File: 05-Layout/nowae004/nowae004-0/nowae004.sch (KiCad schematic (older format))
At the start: 14 parts

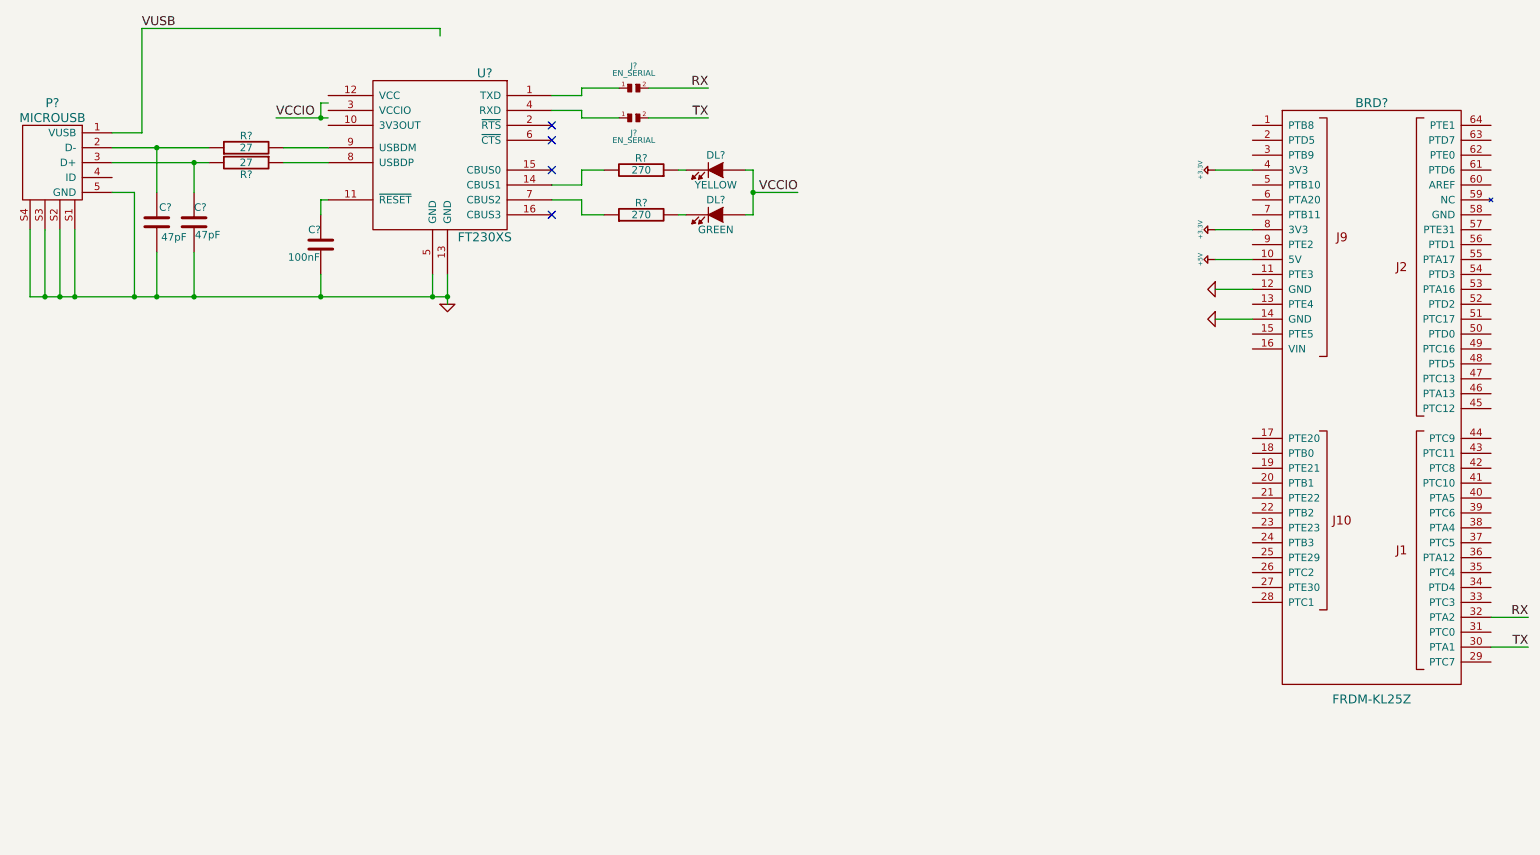
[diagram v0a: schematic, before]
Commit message: Added spare LEDs, protection for power supply and some component informations
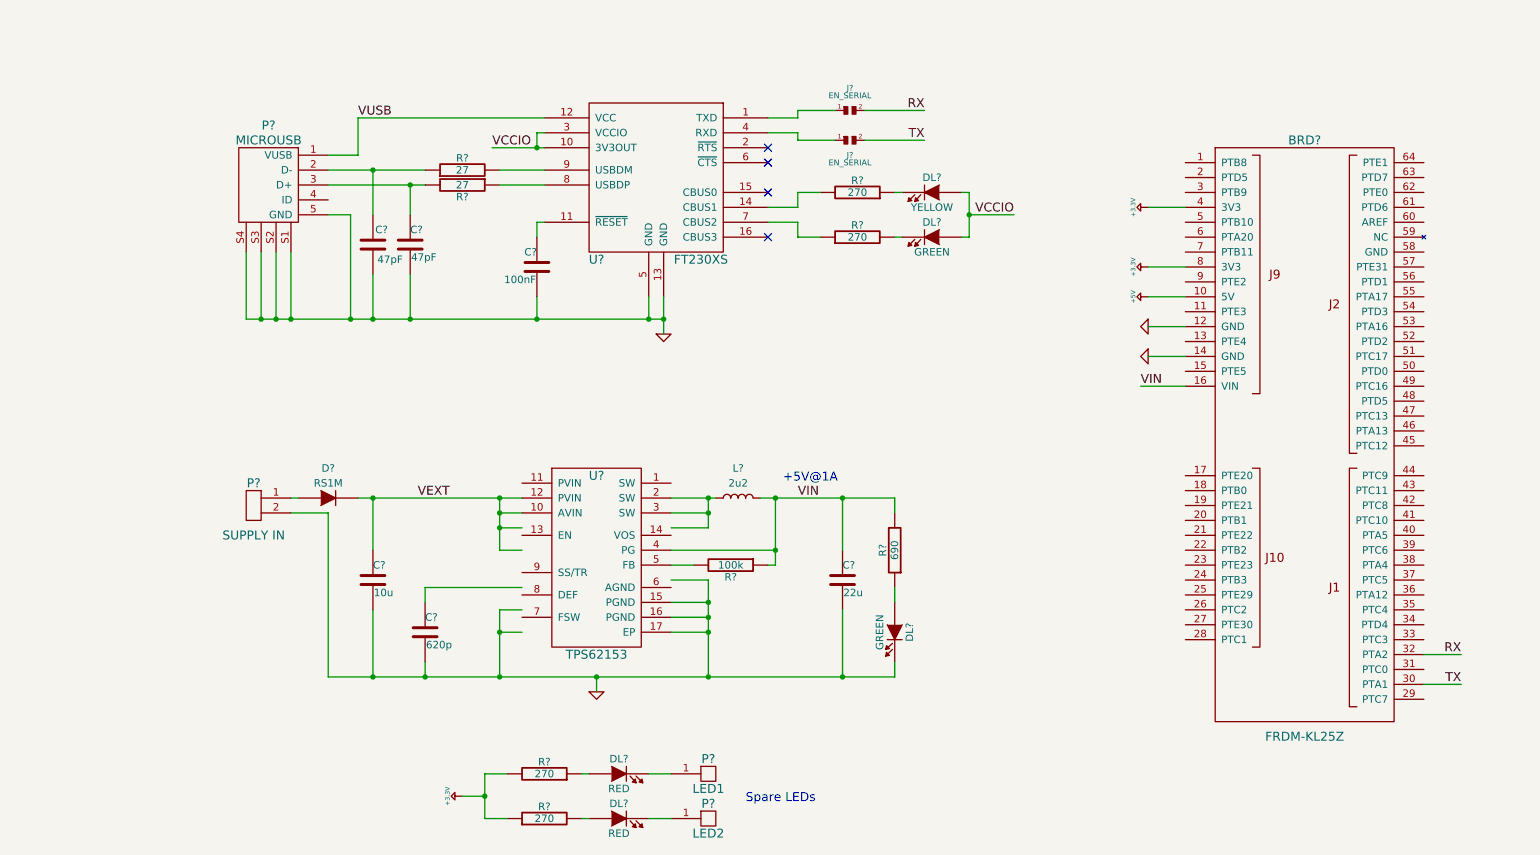
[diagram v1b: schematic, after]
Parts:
- removed U?: FT230XS, SSOP16, symbol FT230XS
- added C?: 10u, 1206, symbol CAPACITOR
- added C?: 620p, 0805, symbol CAPACITOR
- added C?: 22u, 1206, symbol CAPACITOR
- added D?: RS1M, symbol RS1M
- added DL?: GREEN, symbol GREEN
- added DL? (x2): RED, symbol RED
- added L?: 2u2, symbol INDUCTOR
- added P?: SUPPLY IN, symbol CONN_2X1
- added P?: LED1, symbol CONN_1X1
- added P?: LED2, symbol CONN_1X1
- added R?: 100k, symbol RESISTOR
- added R?: 690, symbol RESISTOR
- added R? (x2): 270, symbol RESISTOR
- added U?: TPS62153, VQFN16, symbol TPS62153
- added U?: FT230XS, SSOP16, symbol FT230XS
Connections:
- net labels added: VEXT, VIN
- wire segments 54 -> 132
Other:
- note added: "+5V@1A"
- note added: "Spare LEDs"
- moved on the sheet: BRD?, C?, DL?, J?, P?, R?

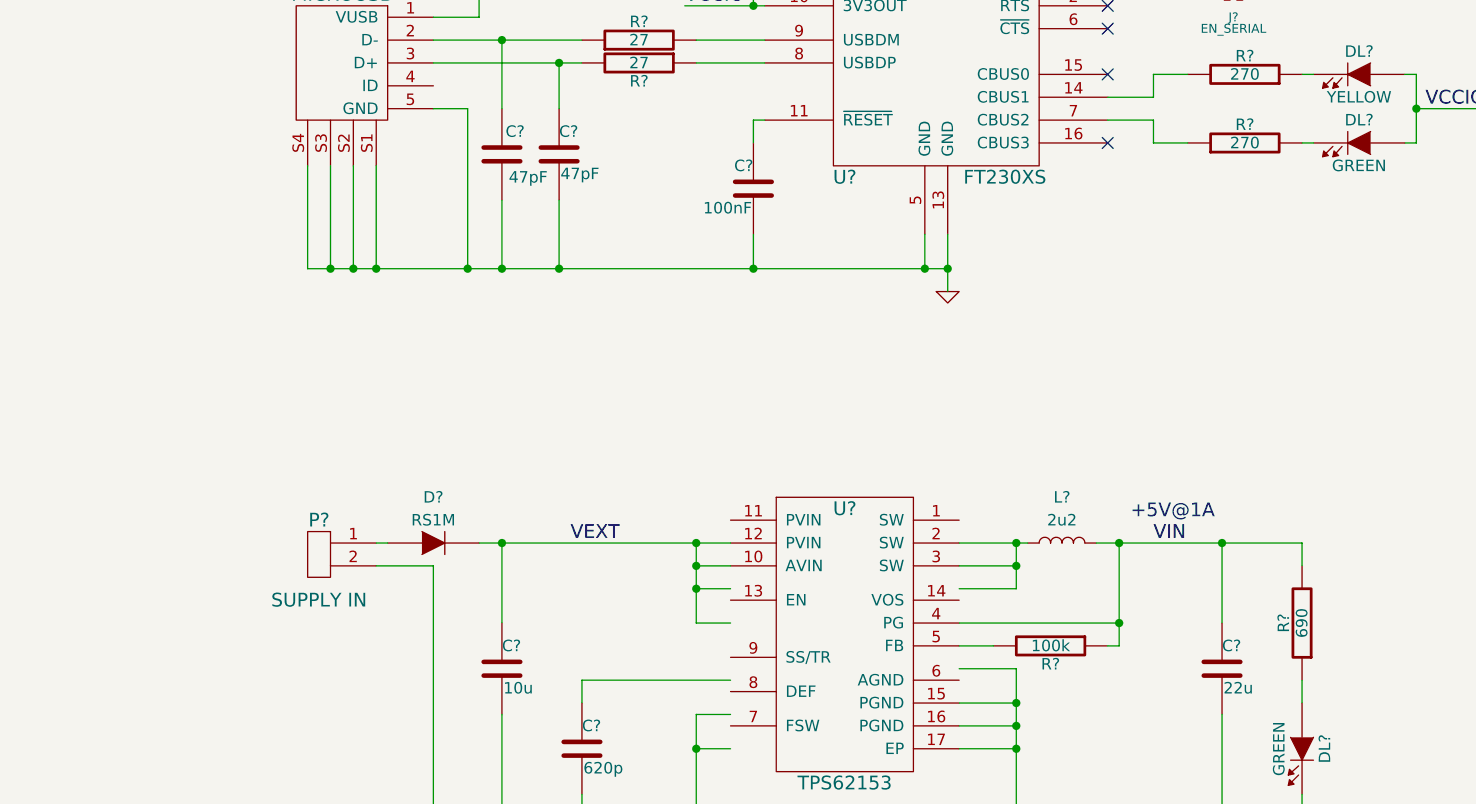
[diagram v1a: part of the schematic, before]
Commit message: Added all component informations. The BOM is complete
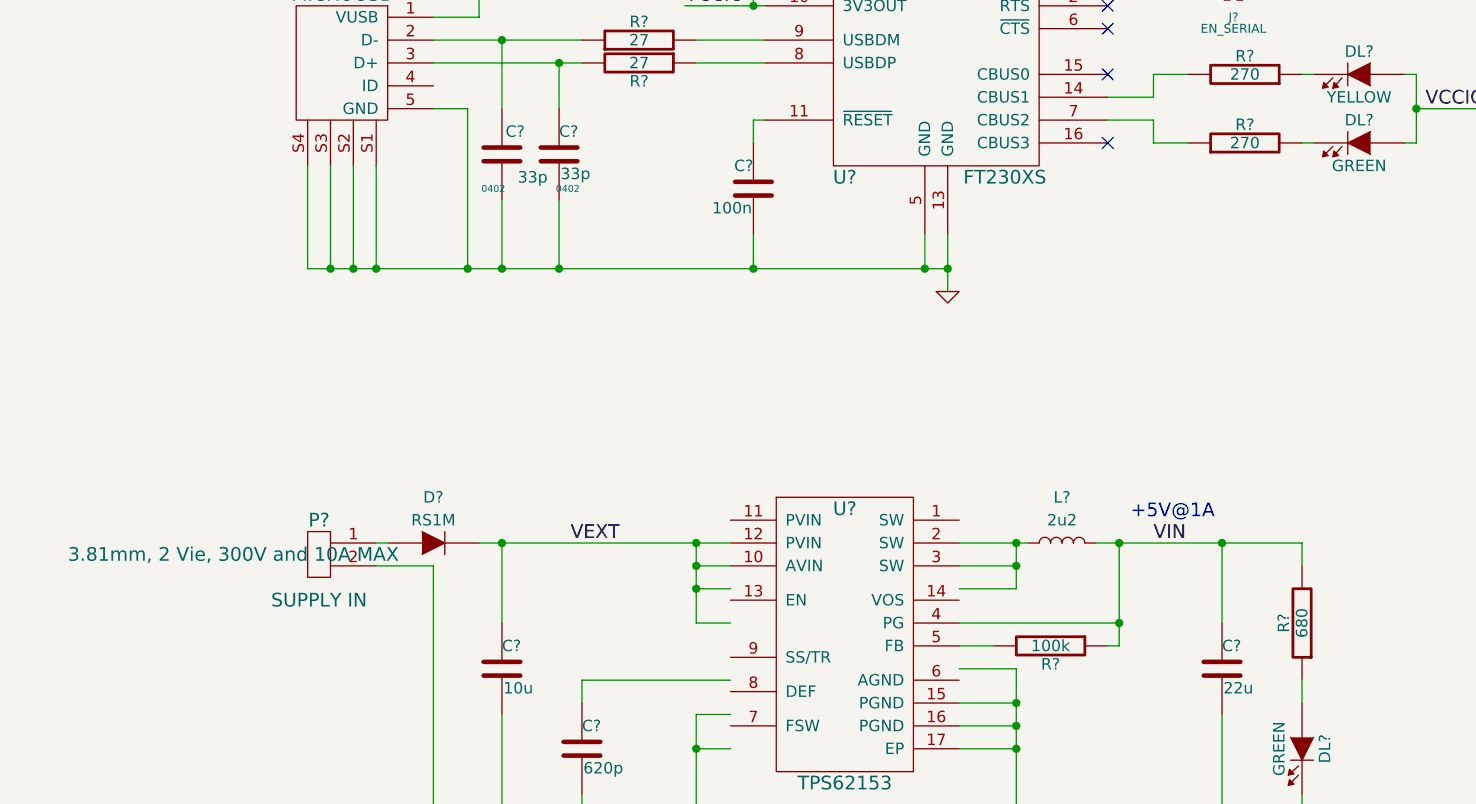
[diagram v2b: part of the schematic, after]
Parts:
- C?: value 100nF -> 100n; footprint (none) -> 0402; Distributor (none) -> Farnell Italia S.r.l.; Distributor Code (none) -> 1758896; Manufacturer (none) -> Multicomp; Part Number (none) -> MC0402B104K160CT; Price € (none) -> 0.005
- C? (x2): value 47pF -> 33p; footprint (none) -> 0402; Distributor (none) -> Farnell Italia S.r.l.; Distributor Code (none) -> 1758955; Manufacturer (none) -> Multicomp; Part Number (none) -> MC0402N330J500CT; Price € (none) -> 0.005
- DL?: footprint (none) -> 0603; Distributor (none) -> Farnell Italia S.r.l.; Distributor Code (none) -> 2099223; Manufacturer (none) -> Kingbright; Part Number (none) -> KPT-1608SGC; Price € (none) -> 0.057
- DL?: Distributor (none) -> Farnell Italia S.r.l.; Distributor Code (none) -> 2099227; Manufacturer (none) -> Kingbright; Part Number (none) -> KPT-1608YC; Price € (none) -> 0.048
- DL?: Distributor (none) -> Farnell Italia S.r.l.; Distributor Code (none) -> 2099223; Manufacturer (none) -> Kingbright; Part Number (none) -> KPT-1608SGC; Price € (none) -> 0.057
- DL? (x2): footprint (none) -> 0603; Distributor (none) -> Farnell Italia S.r.l.; Distributor Code (none) -> 2099221; Manufacturer (none) -> Kingbright; Part Number (none) -> KPT-1608EC; Price € (none) -> 0.064
- P?: Distributor (none) -> Farnell Italia S.r.l.; Distributor Code (none) -> 2007985; Manufacturer (none) -> Multicomp; Part Number (none) -> MC000018; Price € (none) -> 0.791
- R? (x4): footprint (none) -> 0402; Distributor (none) -> Farnell Italia S.r.l.; Distributor Code (none) -> 1358026; Manufacturer (none) -> Multicomp; Part Number (none) -> MC00625W04021270R; Price € (none) -> 0.001
- R? (x2): footprint (none) -> 0402; Distributor (none) -> Farnell Italia S.r.l.; Distributor Code (none) -> 1358000; Manufacturer (none) -> Multicomp; Part Number (none) -> MC00625W0402127R; Price € (none) -> 0.013
- R?: footprint (none) -> 0402; Distributor (none) -> Farnell Italia S.r.l.; Distributor Code (none) -> 1358096; Manufacturer (none) -> Multicomp; Part Number (none) -> MC00625W04021100K; Price € (none) -> 0.001
- R?: value 690 -> 680; footprint (none) -> 0402; Distributor (none) -> Farnell Italia S.r.l.; Distributor Code (none) -> 1358038; Manufacturer (none) -> Multicomp; Part Number (none) -> MC00625W04021680R; Price € (none) -> 0.013
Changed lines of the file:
@@
 F 0 "DL?" H 8500 4100 50  0000 C CNN
 F 1 "GREEN" H 8500 3900 50  0000 C CNN
-F 2 "" H 8500 4000 60  0001 C CNN
+F 2 "0603" H 8500 4000 60  0001 C CNN
 F 3 "Green" H 8500 4000 60  0001 C CNN
+F 4 "Kingbright" H 4550 5950 60  0001 C CNN "Manufacturer"
+F 5 "KPT-1608SGC" H 4650 6050 60  0001 C CNN "Part Number"
+F 6 "Farnell Italia S.r.l." H 4750 6150 60  0001 C CNN "Distributor"
+F 7 "2099223" H 4850 6250 60  0001 C CNN "Distributor Code"
+F 8 "0.057" H 4950 6350 60  0001 C CNN "Price €"
 	1    8500 4000
 	-1   0    0    -1
@@
 F 2 "" H 8500 3700 60  0001 C CNN
 F 3 "Yellow" H 8500 3700 60  0001 C CNN
+F 4 "Kingbright" H 4550 5950 60  0001 C CNN "Manufacturer"
+F 5 "KPT-1608YC" H 4650 6050 60  0001 C CNN "Part Number"
+F 6 "Farnell Italia S.r.l." H 4750 6150 60  0001 C CNN "Distributor"
+F 7 "2099227" H 4850 6250 60  0001 C CNN "Distributor Code"
+F 8 "0.048" H 4950 6350 60  0001 C CNN "Price €"
 	1    8500 3700
 	-1   0    0    -1
@@
 F 0 "R?" V 8080 4000 50  0000 C CNN
 F 1 "270" V 8000 4000 50  0000 C CNN
-F 2 "" V 7930 4000 30  0001 C CNN
+F 2 "0402" V 7930 4000 30  0001 C CNN
 F 3 "" H 8000 4000 30  0001 C CNN
+F 4 "Multicomp" H 4550 5950 60  0001 C CNN "Manufacturer"
+F 5 "MC00625W04021270R" H 4650 6050 60  0001 C CNN "Part Number"
+F 6 "Farnell Italia S.r.l." H 4750 6150 60  0001 C CNN "Distributor"
+F 7 "1358026" H 4850 6250 60  0001 C CNN "Distributor Code"
+F 8 "0.001" H 4950 6350 60  0001 C CNN "Price €"
 	1    8000 4000
 	0    -1   -1   0
@@
 P 5850 4200
 F 0 "C?" H 5850 4300 50  0000 L CNN
-F 1 "100nF" H 5856 4115 50  0000 L CNN
-F 2 "" H 5888 4050 30  0000 C CNN
+F 1 "100n" H 5856 4115 50  0000 L CNN
+F 2 "0402" H 5888 4050 30  0001 C CNN
 F 3 "" H 5850 4200 60  0000 C CNN
+F 4 "Multicomp" H 4550 5950 60  0001 C CNN "Manufacturer"
+F 5 "MC0402B104K160CT" H 4650 6050 60  0001 C CNN "Part Number"
+F 6 "Farnell Italia S.r.l." H 4750 6150 60  0001 C CNN "Distributor"
+F 7 "1758896" H 4850 6250 60  0001 C CNN "Distributor Code"
+F 8 "0.005" H 4950 6350 60  0001 C CNN "Price €"
 	1    5850 4200
 	-1   0    0    -1
@@
 F 0 "R?" V 5430 3650 50  0000 C CNN
 F 1 "27" V 5350 3650 50  0000 C CNN
-F 2 "" V 5280 3650 30  0001 C CNN
+F 2 "0402" V 5280 3650 30  0001 C CNN
 F 3 "" H 5350 3650 30  0001 C CNN
+F 4 "Multicomp" H 4550 5950 60  0001 C CNN "Manufacturer"
+F 5 "MC00625W0402127R" H 4650 6050 60  0001 C CNN "Part Number"
+F 6 "Farnell Italia S.r.l." H 4750 6150 60  0001 C CNN "Distributor"
+F 7 "1358000" H 4850 6250 60  0001 C CNN "Distributor Code"
+F 8 "0.013" H 4950 6350 60  0001 C CNN "Price €"
 	1    5350 3650
 	0    1    1    0
@@
 F 0 "R?" V 5430 3550 50  0000 C CNN
 F 1 "27" V 5350 3550 50  0000 C CNN
-F 2 "" V 5280 3550 30  0001 C CNN
+F 2 "0402" V 5280 3550 30  0001 C CNN
 F 3 "" H 5350 3550 30  0001 C CNN
+F 4 "Multicomp" H 4550 5950 60  0001 C CNN "Manufacturer"
+F 5 "MC00625W0402127R" H 4650 6050 60  0001 C CNN "Part Number"
+F 6 "Farnell Italia S.r.l." H 4750 6150 60  0001 C CNN "Distributor"
+F 7 "1358000" H 4850 6250 60  0001 C CNN "Distributor Code"
+F 8 "0.013" H 4950 6350 60  0001 C CNN "Price €"
 	1    5350 3550
 	0    -1   -1   0
@@
 P 5000 4050
 F 0 "C?" H 5000 4150 50  0000 L CNN
-F 1 "47pF" H 5006 3965 50  0000 L CNN
-F 2 "" H 5038 3900 30  0000 C CNN
+F 1 "33p" H 5006 3965 50  0000 L CNN
+F 2 "0402" H 5038 3900 30  0000 C CNN
 F 3 "" H 5000 4050 60  0000 C CNN
+F 4 "Multicomp" H 4550 5950 60  0001 C CNN "Manufacturer"
+F 5 "MC0402N330J500CT" H 4650 6050 60  0001 C CNN "Part Number"
+F 6 "Farnell Italia S.r.l." H 4750 6150 60  0001 C CNN "Distributor"
+F 7 "1758955" H 4850 6250 60  0001 C CNN "Distributor Code"
+F 8 "0.005" H 4950 6350 60  0001 C CNN "Price €"
 	1    5000 4050
 	1    0    0    -1
@@
 P 4750 4050
 F 0 "C?" H 4650 4150 50  0000 L CNN
-F 1 "47pF" H 4550 3950 50  0000 L CNN
-F 2 "" H 4788 3900 30  0000 C CNN
+F 1 "33p" H 4550 3950 50  0000 L CNN
+F 2 "0402" H 4788 3900 30  0000 C CNN
 F 3 "" H 4750 4050 60  0000 C CNN
+F 4 "Multicomp" H 4550 5950 60  0001 C CNN "Manufacturer"
+F 5 "MC0402N330J500CT" H 4650 6050 60  0001 C CNN "Part Number"
+F 6 "Farnell Italia S.r.l." H 4750 6150 60  0001 C CNN "Distributor"
+F 7 "1758955" H 4850 6250 60  0001 C CNN "Distributor Code"
+F 8 "0.005" H 4950 6350 60  0001 C CNN "Price €"
 	1    4750 4050
 	-1   0    0    -1
@@
 F 0 "R?" V 8080 3700 50  0000 C CNN
 F 1 "270" V 8000 3700 50  0000 C CNN
-F 2 "" V 7930 3700 30  0001 C CNN
+F 2 "0402" V 7930 3700 30  0001 C CNN
 F 3 "" H 8000 3700 30  0001 C CNN
+F 4 "Multicomp" H 4550 5950 60  0001 C CNN "Manufacturer"
+F 5 "MC00625W04021270R" H 4650 6050 60  0001 C CNN "Part Number"
+F 6 "Farnell Italia S.r.l." H 4750 6150 60  0001 C CNN "Distributor"
+F 7 "1358026" H 4850 6250 60  0001 C CNN "Distributor Code"
+F 8 "0.001" H 4950 6350 60  0001 C CNN "Price €"
 	1    8000 3700
 	0    1    -1   0
@@
 F 1 "SUPPLY IN" H 3950 5600 60  0000 C CNN
 F 2 "" H 4325 5800 60  0000 C CNN
-F 3 "" H 4325 5800 60  0000 C CNN
+F 3 "3.81mm, 2 Vie, 300V and 10A MAX " H 4325 5800 60  0000 C CNN
+F 4 "Multicomp" H 4550 5950 60  0001 C CNN "Manufacturer"
+F 5 "MC000018" H 4650 6050 60  0001 C CNN "Part Number"
+F 6 "Farnell Italia S.r.l." H 4750 6150 60  0001 C CNN "Distributor"
+F 7 "2007985" H 4850 6250 60  0001 C CNN "Distributor Code"
+F 8 "0.791" H 4950 6350 60  0001 C CNN "Price €"
 	1    3950 5800
 	-1   0    0    -1
@@
 F 0 "R?" V 7230 6200 50  0000 C CNN
 F 1 "100k" V 7150 6200 50  0000 C CNN
-F 2 "" V 7080 6200 30  0001 C CNN
+F 2 "0402" V 7080 6200 30  0001 C CNN
 F 3 "" H 7150 6200 30  0001 C CNN
+F 4 "Multicomp" H 4550 5950 60  0001 C CNN "Manufacturer"
+F 5 "MC00625W04021100K" H 4650 6050 60  0001 C CNN "Part Number"
+F 6 "Farnell Italia S.r.l." H 4750 6150 60  0001 C CNN "Distributor"
+F 7 "1358096" H 4850 6250 60  0001 C CNN "Distributor Code"
+F 8 "0.001" H 4950 6350 60  0001 C CNN "Price €"
 	1    7150 6200
 	0    1    1    0
@@
 P 8250 6100
 F 0 "R?" V 8330 6100 50  0000 C CNN
-F 1 "690" V 8250 6100 50  0000 C CNN
-F 2 "" V 8180 6100 30  0001 C CNN
+F 1 "680" V 8250 6100 50  0000 C CNN
+F 2 "0402" V 8180 6100 30  0001 C CNN
 F 3 "" H 8250 6100 30  0001 C CNN
+F 4 "Multicomp" H 4550 5950 60  0001 C CNN "Manufacturer"
+F 5 "MC00625W04021680R" H 4650 6050 60  0001 C CNN "Part Number"
+F 6 "Farnell Italia S.r.l." H 4750 6150 60  0001 C CNN "Distributor"
+F 7 "1358038" H 4850 6250 60  0001 C CNN "Distributor Code"
+F 8 "0.013" H 4950 6350 60  0001 C CNN "Price €"
 	1    8250 6100
 	-1   0    0    1
@@
 F 2 "" H 8250 6650 60  0001 C CNN
 F 3 "Green" H 8250 6650 60  0001 C CNN
+F 4 "Kingbright" H 4550 5950 60  0001 C CNN "Manufacturer"
+F 5 "KPT-1608SGC" H 4650 6050 60  0001 C CNN "Part Number"
+F 6 "Farnell Italia S.r.l." H 4750 6150 60  0001 C CNN "Distributor"
+F 7 "2099223" H 4850 6250 60  0001 C CNN "Distributor Code"
+F 8 "0.057" H 4950 6350 60  0001 C CNN "Price €"
 	1    8250 6650
 	0    1    1    0
@@
 F 0 "R?" V 5980 7900 50  0000 C CNN
 F 1 "270" V 5900 7900 50  0000 C CNN
-F 2 "" V 5830 7900 30  0001 C CNN
+F 2 "0402" V 5830 7900 30  0001 C CNN
 F 3 "" H 5900 7900 30  0001 C CNN
+F 4 "Multicomp" H 4550 5950 60  0001 C CNN "Manufacturer"
+F 5 "MC00625W04021270R" H 4650 6050 60  0001 C CNN "Part Number"
+F 6 "Farnell Italia S.r.l." H 4750 6150 60  0001 C CNN "Distributor"
+F 7 "1358026" H 4850 6250 60  0001 C CNN "Distributor Code"
+F 8 "0.001" H 4950 6350 60  0001 C CNN "Price €"
 	1    5900 7900
 	0    -1   -1   0
@@
 F 0 "R?" V 5980 7600 50  0000 C CNN
 F 1 "270" V 5900 7600 50  0000 C CNN
-F 2 "" V 5830 7600 30  0001 C CNN
+F 2 "0402" V 5830 7600 30  0001 C CNN
 F 3 "" H 5900 7600 30  0001 C CNN
+F 4 "Multicomp" H 4550 5950 60  0001 C CNN "Manufacturer"
+F 5 "MC00625W04021270R" H 4650 6050 60  0001 C CNN "Part Number"
+F 6 "Farnell Italia S.r.l." H 4750 6150 60  0001 C CNN "Distributor"
+F 7 "1358026" H 4850 6250 60  0001 C CNN "Distributor Code"
+F 8 "0.001" H 4950 6350 60  0001 C CNN "Price €"
 	1    5900 7600
 	0    1    -1   0
@@
 F 0 "DL?" H 6400 7700 50  0000 C CNN
 F 1 "RED" H 6400 7500 50  0000 C CNN
-F 2 "" H 6400 7600 60  0001 C CNN
+F 2 "0603" H 6400 7600 60  0001 C CNN
 F 3 "Red" H 6400 7600 60  0001 C CNN
+F 4 "Kingbright" H 4550 5950 60  0001 C CNN "Manufacturer"
+F 5 "KPT-1608EC" H 4650 6050 60  0001 C CNN "Part Number"
+F 6 "Farnell Italia S.r.l." H 4750 6150 60  0001 C CNN "Distributor"
+F 7 "2099221" H 4850 6250 60  0001 C CNN "Distributor Code"
+F 8 "0.064" H 4950 6350 60  0001 C CNN "Price €"
 	1    6400 7600
 	1    0    0    -1
@@
 F 0 "DL?" H 6400 8000 50  0000 C CNN
 F 1 "RED" H 6400 7800 50  0000 C CNN
-F 2 "" H 6400 7900 60  0001 C CNN
+F 2 "0603" H 6400 7900 60  0001 C CNN
 F 3 "Red" H 6400 7900 60  0001 C CNN
+F 4 "Kingbright" H 4550 5950 60  0001 C CNN "Manufacturer"
+F 5 "KPT-1608EC" H 4650 6050 60  0001 C CNN "Part Number"
+F 6 "Farnell Italia S.r.l." H 4750 6150 60  0001 C CNN "Distributor"
+F 7 "2099221" H 4850 6250 60  0001 C CNN "Distributor Code"
+F 8 "0.064" H 4950 6350 60  0001 C CNN "Price €"
 	1    6400 7900
 	1    0    0    -1
@@
 F 0 "P?" H 7000 8000 60  0000 C CNN
 F 1 "LED2" H 7000 7800 60  0000 C CNN
-F 2 "" H 7375 7900 60  0000 C CNN
+F 2 "" H 7000 7700 60  0001 C CNN
 F 3 "" H 7375 7900 60  0000 C CNN
 	1    7000 7900
